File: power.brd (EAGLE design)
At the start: 73.3 x 52.1 mm, 21 parts

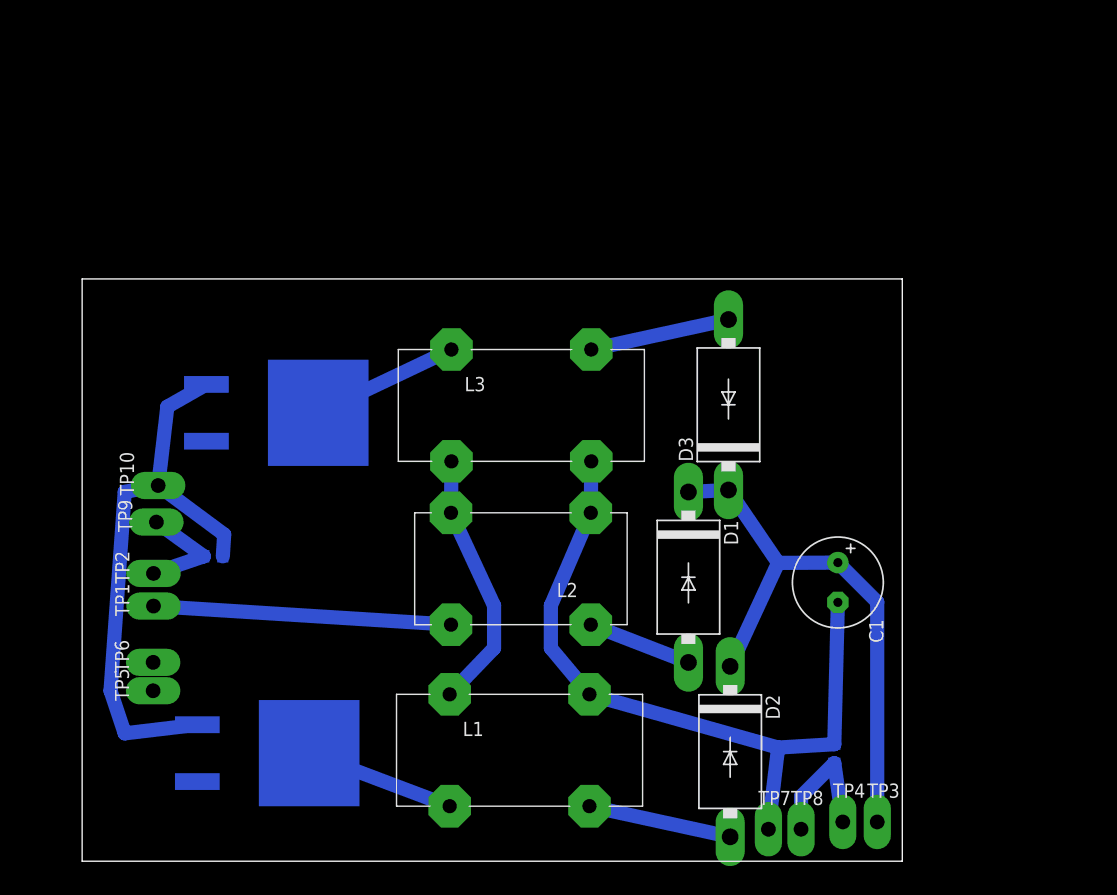
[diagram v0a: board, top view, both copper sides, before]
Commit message: Transformer footprints and really awful looking board routing
Pretty sure at least one of the transformers is wired in the wrong way
too
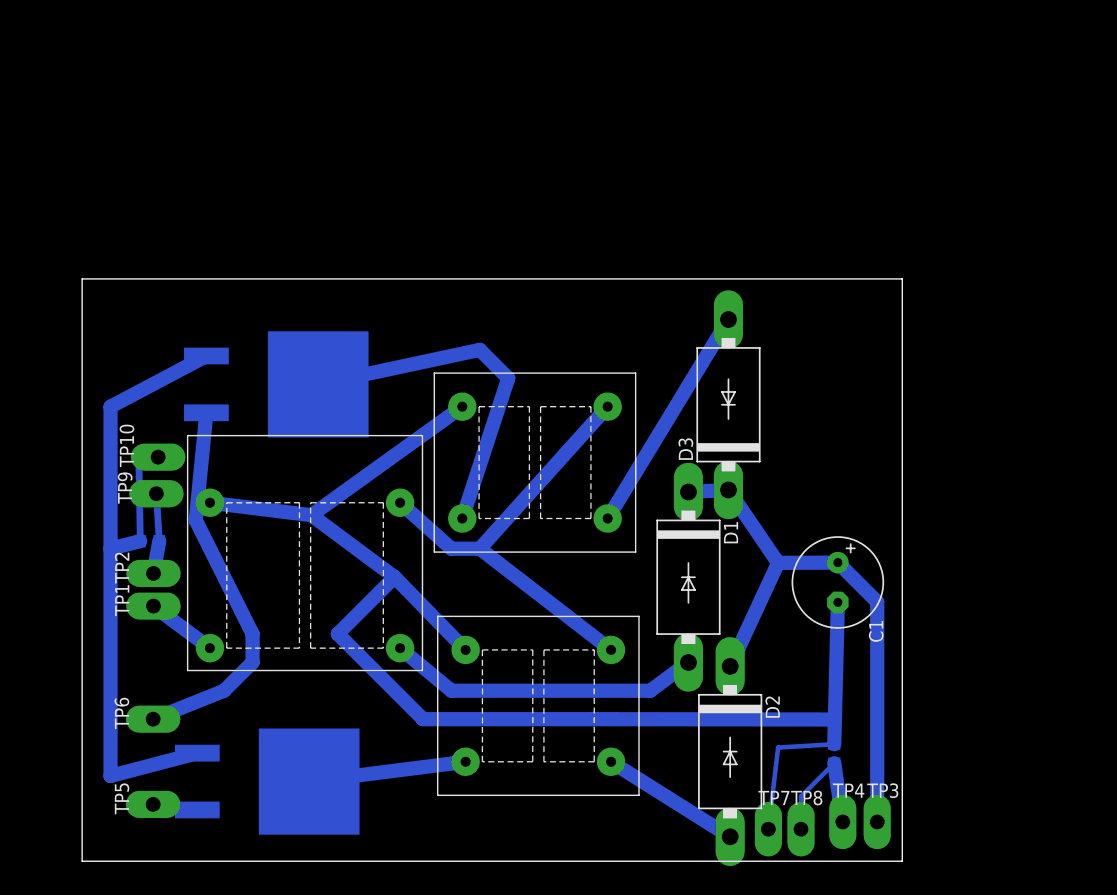
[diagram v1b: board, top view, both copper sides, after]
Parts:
- removed L1, L3: (no value), inductor-nkl:B2
- removed L2: (no value), inductor-nkl:B1
- added U$3: PLH10AN2211R5P2B, chokes:L13-17
- added U$4, U$5: TLF14CBH3321R0K1, chokes:L10-13
- moved TP5 10.2 mm to (1.27, 5.08)
- moved R2 5.84 mm to (0.97, 28.6), turned to 0 degrees
- moved TP6 5.08 mm to (1.27, 12.7)
- moved U$1 2.54 mm to (15.2, 7.12)
- moved TP10 2.54 mm to (1.72, 36.1)
- moved TP9 2.54 mm to (1.56, 32.9)
- moved U$2 2.54 mm to (16.0, 42.6)
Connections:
- removed net N$7: D2.A, L1.4
- new net N$15: U$1.P$3, U$5.P$1
- net N$1: now also U$3.P$2; no longer L2.1
- net N$2: now also D2.A, U$5.P$2; no longer L1.1, L2.4, L3.2
- net N$3: now also U$3.P$1; no longer L2.3
- net N$4: now also U$3.P$4, U$4.P$2, U$5.P$4; no longer L1.3, L2.2, L3.4
- net N$5: now also U$4.P$3; no longer L3.1
- net N$6: now also U$3.P$3, U$4.P$1, U$5.P$3; no longer L1.2, U$1.P$3
- net N$9: now also U$4.P$4; no longer L3.3
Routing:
- net N$4: track 65.4 -> 124.0 mm
- net N$13: track 0.00 -> 34.0 mm
- net N$6: track 13.4 -> 40.6 mm
- net N$3: track 26.7 -> 6.30 mm
- net N$1: track 9.36 -> 28.0 mm
- net N$5: track 13.2 -> 31.6 mm
- net N$15: track 0.00 -> 14.1 mm
- net N$7: track 12.9 -> 0.00 mm
- net N$2: track 23.3 -> 12.6 mm
- net N$11: track 51.8 -> 62.2 mm
- net N$9: track 12.6 -> 20.8 mm
- net N$10: track 9.98 -> 7.18 mm

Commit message: little tweaks
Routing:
- net N$4: track 124.0 -> 119.1 mm
- net N$12: track 0.00 -> 3.98 mm
- net N$11: track 62.2 -> 59.4 mm
- net N$6: track 40.6 -> 39.6 mm
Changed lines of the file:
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@@
 <wire x1="62.49" y1="23.142" x2="62.225715625" y2="12.6680625" width="1.27" layer="16"/>
 <wire x1="62.225715625" y1="12.6680625" x2="62.17" y2="10.46" width="1.27" layer="16"/>
-<wire x1="62.17" y1="10.46" x2="57.15" y2="10.16" width="0.4064" layer="16"/>
-<wire x1="57.15" y1="10.16" x2="56.28" y2="2.86" width="0.4064" layer="16"/>
+<wire x1="62.17" y1="10.46" x2="57.15" y2="7.62" width="0.4064" layer="16"/>
+<wire x1="57.15" y1="7.62" x2="56.28" y2="2.86" width="0.4064" layer="16"/>
 <contactref element="U$3" pad="P$4"/>
 <contactref element="U$5" pad="P$4"/>
 <contactref element="U$4" pad="P$2"/>
-<wire x1="29.21" y1="18.89" x2="22.86" y2="25.4" width="1.27" layer="16"/>
-<wire x1="22.86" y1="25.4" x2="15.423409375" y2="30.93535625" width="1.27" layer="16"/>
-<wire x1="15.423409375" y1="30.93535625" x2="6.35" y2="32.05" width="1.27" layer="16"/>
-<wire x1="28.91" y1="40.64" x2="15.423409375" y2="30.93535625" width="1.27" layer="16"/>
+<wire x1="29.21" y1="18.89" x2="20.32" y2="25.4" width="1.27" layer="16"/>
+<wire x1="20.32" y1="25.4" x2="17.963409375" y2="33.47535625" width="1.27" layer="16"/>
+<wire x1="17.963409375" y1="33.47535625" x2="6.35" y2="32.05" width="1.27" layer="16"/>
+<wire x1="28.91" y1="40.64" x2="17.963409375" y2="33.47535625" width="1.27" layer="16"/>
 <wire x1="40.64" y1="12.7" x2="25.4" y2="12.7" width="1.27" layer="16"/>
-<wire x1="25.4" y1="12.7" x2="17.78" y2="20.32" width="1.27" layer="16"/>
-<wire x1="17.78" y1="20.32" x2="22.86" y2="25.4" width="1.27" layer="16"/>
+<wire x1="25.4" y1="12.7" x2="20.32" y2="17.78" width="1.27" layer="16"/>
+<wire x1="20.32" y1="17.78" x2="20.32" y2="25.4" width="1.27" layer="16"/>
 <wire x1="40.64" y1="12.7" x2="62.225715625" y2="12.6680625" width="1.27" layer="16"/>
 </signal>
@@
 <contactref element="R2" pad="2"/>
 <contactref element="TP10" pad="TP"/>
-<wire x1="5.22" y1="9.66" x2="-2.54" y2="7.62" width="1.27" layer="16"/>
-<wire x1="-2.54" y1="7.62" x2="-2.54" y2="27.94" width="1.27" layer="16"/>
+<wire x1="5.22" y1="9.66" x2="-2.54" y2="10.16" width="1.27" layer="16"/>
+<wire x1="-2.54" y1="10.16" x2="-2.54" y2="27.94" width="1.27" layer="16"/>
 <wire x1="-2.54" y1="27.94" x2="-2.54" y2="40.64" width="1.27" layer="16"/>
 <wire x1="-2.54" y1="40.64" x2="6.03" y2="45.17" width="1.27" layer="16"/>
 <wire x1="0.12" y1="28.62" x2="-2.54" y2="27.94" width="1.27" layer="16"/>
-<wire x1="1.72" y1="36.13" x2="0" y2="35.56" width="0.6096" layer="16"/>
-<wire x1="0" y1="35.56" x2="0.12" y2="28.62" width="0.6096" layer="16"/>
+<wire x1="1.72" y1="36.13" x2="0" y2="35.56" width="0.4064" layer="16"/>
+<wire x1="0" y1="35.56" x2="0.12" y2="28.62" width="0.4064" layer="16"/>
 </signal>
 <signal name="N$12">
 <contactref element="TP5" pad="TP"/>
 <contactref element="U$1" pad="P$1"/>
-<wire x1="5.22" y1="4.58" x2="1.27" y2="5.08" width="0" layer="19" extent="16-16"/>
+<wire x1="1.27" y1="5.08" x2="5.22" y2="4.58" width="0.4064" layer="16"/>
 </signal>
 <signal name="N$13">
 <contactref element="TP6" pad="TP"/>
 <contactref element="U$2" pad="P$1"/>
-<wire x1="1.27" y1="12.7" x2="7.62" y2="15.24" width="1.27" layer="16"/>
-<wire x1="7.62" y1="15.24" x2="10.16" y2="17.78" width="1.27" layer="16"/>
-<wire x1="10.16" y1="17.78" x2="10.16" y2="20.32" width="1.27" layer="16"/>
-<wire x1="10.16" y1="20.32" x2="5.08" y2="30.48" width="1.27" layer="16"/>
-<wire x1="5.08" y1="30.48" x2="6.03" y2="40.09" width="1.27" layer="16"/>
+<wire x1="1.27" y1="12.7" x2="7.62" y2="15.24" width="0.4064" layer="16"/>
+<wire x1="7.62" y1="15.24" x2="10.16" y2="17.78" width="0.4064" layer="16"/>
+<wire x1="10.16" y1="17.78" x2="10.16" y2="20.32" width="0.4064" layer="16"/>
+<wire x1="10.16" y1="20.32" x2="5.08" y2="30.48" width="0.4064" layer="16"/>
+<wire x1="5.08" y1="30.48" x2="6.03" y2="40.09" width="0.4064" layer="16"/>
 </signal>
 <signal name="N$14">
@@
 <contactref element="TP2" pad="TP"/>
 <wire x1="1.3" y1="25.73" x2="1.82" y2="28.62" width="1.27" layer="16"/>
-<wire x1="1.56" y1="32.86" x2="1.82" y2="28.62" width="0.6096" layer="16"/>
+<wire x1="1.56" y1="32.86" x2="1.82" y2="28.62" width="0.4064" layer="16"/>
 </signal>
 <signal name="N$1">
@@
 <contactref element="U$4" pad="P$1"/>
 <wire x1="23.35" y1="32.05" x2="27.94" y2="27.94" width="1.27" layer="16"/>
-<wire x1="27.94" y1="27.94" x2="30.48" y2="27.94" width="1.27" layer="16"/>
-<wire x1="30.48" y1="27.94" x2="41.91" y2="40.64" width="1.27" layer="16"/>
-<wire x1="42.21" y1="18.89" x2="30.48" y2="27.94" width="1.27" layer="16"/>
+<wire x1="27.94" y1="27.94" x2="33.02" y2="27.94" width="1.27" layer="16"/>
+<wire x1="33.02" y1="27.94" x2="41.91" y2="40.64" width="1.27" layer="16"/>
+<wire x1="42.21" y1="18.89" x2="33.02" y2="27.94" width="1.27" layer="16"/>
 </signal>
 </signals>

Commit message: fiddling with the layout
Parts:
- moved TP3 7.62 mm to (66.0, 11.1)
- moved D3 5.68 mm to (55.2, 35.7)
- moved D2 5.68 mm to (55.4, 14.9)
- moved TP4 3.59 mm to (65.5, 6.05)
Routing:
- net N$8: track 51.7 -> 37.1 mm
- net N$9: track 20.8 -> 18.4 mm
- net N$14: track 12.4 -> 11.4 mm
- net N$2: track 12.6 -> 13.3 mm
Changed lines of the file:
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@@
 <?xml version="1.0" encoding="utf-8"?>
 <!DOCTYPE eagle SYSTEM "eagle.dtd">
-<eagle version="6.5.1">
+<eagle version="6.5.0">
 <drawing>
 <settings>
@@
 <setting verticaltext="up"/>
 </settings>
-<grid distance="0.1" unitdist="inch" unit="inch" style="lines" multiple="1" display="yes" altdistance="0.5" altunitdist="mm" altunit="mm"/>
+<grid distance="1" unitdist="mm" unit="mm" style="lines" multiple="5" display="yes" altdistance="0.5" altunitdist="mm" altunit="mm"/>
 <layers>
 <layer number="1" name="Top" color="4" fill="1" visible="yes" active="yes"/>
@@
 <attribute name="TP_SIGNAL_NAME" value="" x="19.08" y="47.32" size="1.778" layer="27" rot="R90" display="off"/>
 </element>
-<element name="TP3" library="testpad" package="P1-13Y" value="TPPAD1-13Y" x="66.01" y="3.51">
-<attribute name="TP_SIGNAL_NAME" value="" x="92.68" y="-14.27" size="1.778" layer="27" display="off"/>
-</element>
-<element name="TP4" library="testpad" package="P1-13Y" value="TPPAD1-13Y" x="62.93" y="3.51">
-<attribute name="TP_SIGNAL_NAME" value="" x="94.68" y="-14.27" size="1.778" layer="27" display="off"/>
+<element name="TP3" library="testpad" package="P1-13Y" value="TPPAD1-13Y" x="66.01" y="11.13">
+<attribute name="TP_SIGNAL_NAME" value="" x="92.68" y="-6.65" size="1.778" layer="27" display="off"/>
+</element>
+<element name="TP4" library="testpad" package="P1-13Y" value="TPPAD1-13Y" x="65.47" y="6.05">
+<attribute name="TP_SIGNAL_NAME" value="" x="97.22" y="-11.73" size="1.778" layer="27" display="off"/>
 </element>
 <element name="TP5" library="testpad" package="P1-13Y" value="TPPAD1-13Y" x="1.27" y="5.08" rot="R90">
@@
 </element>
 <element name="D1" library="diode" package="DO201-15" value="BY500" x="49.13" y="25.39" rot="R270"/>
-<element name="D2" library="diode" package="DO201-15" value="BY500" x="52.86" y="9.8" rot="R270"/>
-<element name="D3" library="diode" package="DO201-15" value="BY500" x="52.71" y="40.81" rot="R90"/>
+<element name="D2" library="diode" package="DO201-15" value="BY500" x="55.4" y="14.88" rot="R270"/>
+<element name="D3" library="diode" package="DO201-15" value="BY500" x="55.25" y="35.73" rot="R90"/>
 <element name="C1" library="rcl" package="E3,5-8" value="" x="62.49" y="24.92" rot="R270"/>
 <element name="U$1" library="mjg" package="TO-263AB" value="FDB6670AL" x="15.22" y="7.12" rot="MR90"/>
@@
 <contactref element="C1" pad="+"/>
 <contactref element="D3" pad="C"/>
-<wire x1="49.13" y1="33.01" x2="52.71" y2="33.19" width="1.27" layer="16"/>
+<wire x1="49.13" y1="33.01" x2="55.25" y2="28.11" width="1.27" layer="16"/>
 <wire x1="62.49" y1="26.698" x2="66.01" y2="23.178" width="1.27" layer="16"/>
-<wire x1="66.01" y1="23.178" x2="66.01" y2="3.51" width="1.27" layer="16"/>
-<wire x1="52.71" y1="33.19" x2="57.15" y2="26.67" width="1.27" layer="16"/>
-<wire x1="57.15" y1="26.67" x2="52.86" y2="17.42" width="1.27" layer="16"/>
+<wire x1="66.01" y1="23.178" x2="66.01" y2="11.13" width="1.27" layer="16"/>
+<wire x1="55.25" y1="28.11" x2="57.15" y2="26.67" width="1.27" layer="16"/>
+<wire x1="57.15" y1="26.67" x2="55.4" y2="22.5" width="1.27" layer="16"/>
 <wire x1="57.15" y1="26.67" x2="62.49" y2="26.698" width="1.27" layer="16"/>
 </signal>
@@
 <contactref element="D3" pad="A"/>
 <contactref element="U$4" pad="P$4"/>
-<wire x1="41.91" y1="30.64" x2="52.71" y2="48.43" width="1.27" layer="16"/>
+<wire x1="41.91" y1="30.64" x2="55.25" y2="43.35" width="1.27" layer="16"/>
 </signal>
 <signal name="N$5">
@@
 <contactref element="R1" pad="2"/>
 <contactref element="TP8" pad="TP"/>
-<wire x1="62.17" y1="8.76" x2="62.93" y2="3.51" width="1.27" layer="16"/>
+<wire x1="62.17" y1="8.76" x2="65.47" y2="6.05" width="1.27" layer="16"/>
 <wire x1="59.2" y1="2.86" x2="59.2" y2="5.79" width="0.4064" layer="16"/>
 <wire x1="59.2" y1="5.79" x2="62.17" y2="8.76" width="0.4064" layer="16"/>
@@
 <contactref element="D2" pad="A"/>
 <contactref element="U$5" pad="P$2"/>
-<wire x1="52.86" y1="2.18" x2="42.21" y2="8.89" width="1.27" layer="16"/>
+<wire x1="55.4" y1="7.26" x2="42.21" y2="8.89" width="1.27" layer="16"/>
 </signal>
 <signal name="N$15">

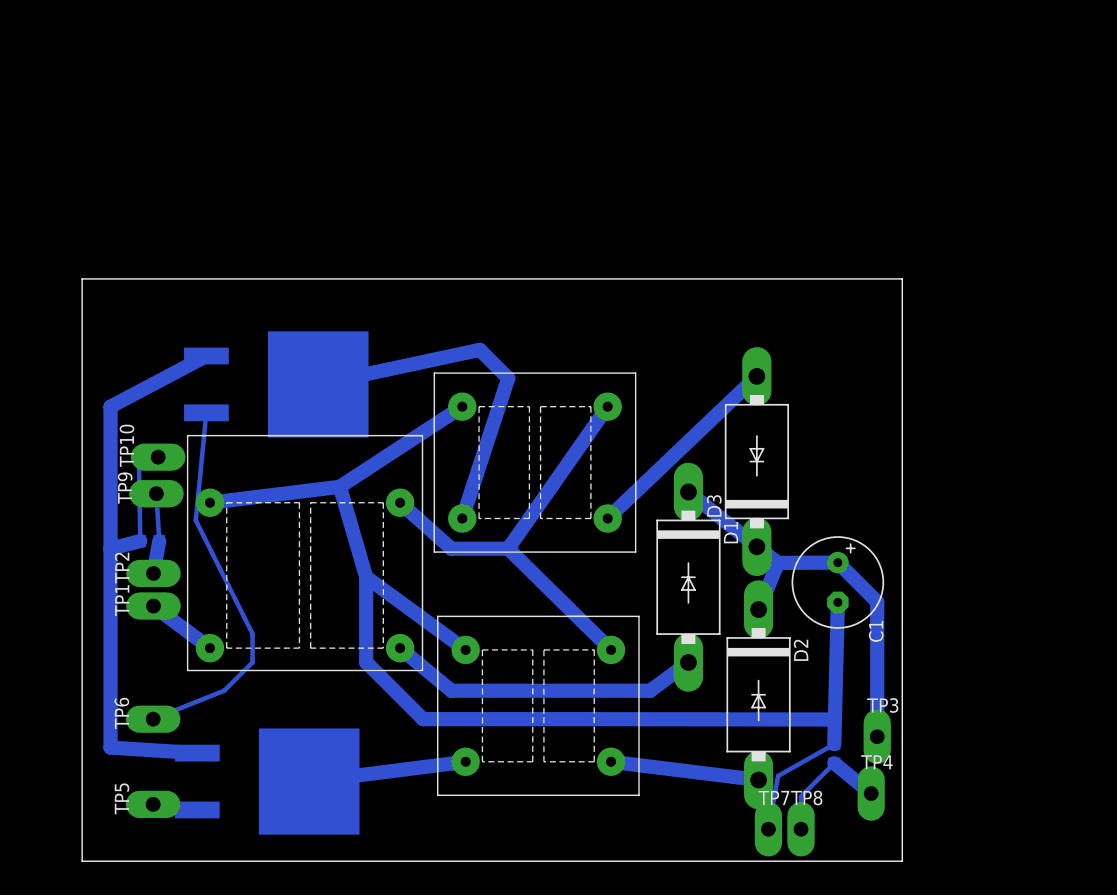
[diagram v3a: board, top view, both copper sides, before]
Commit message: proposed beaglebone connections and resistor dividers
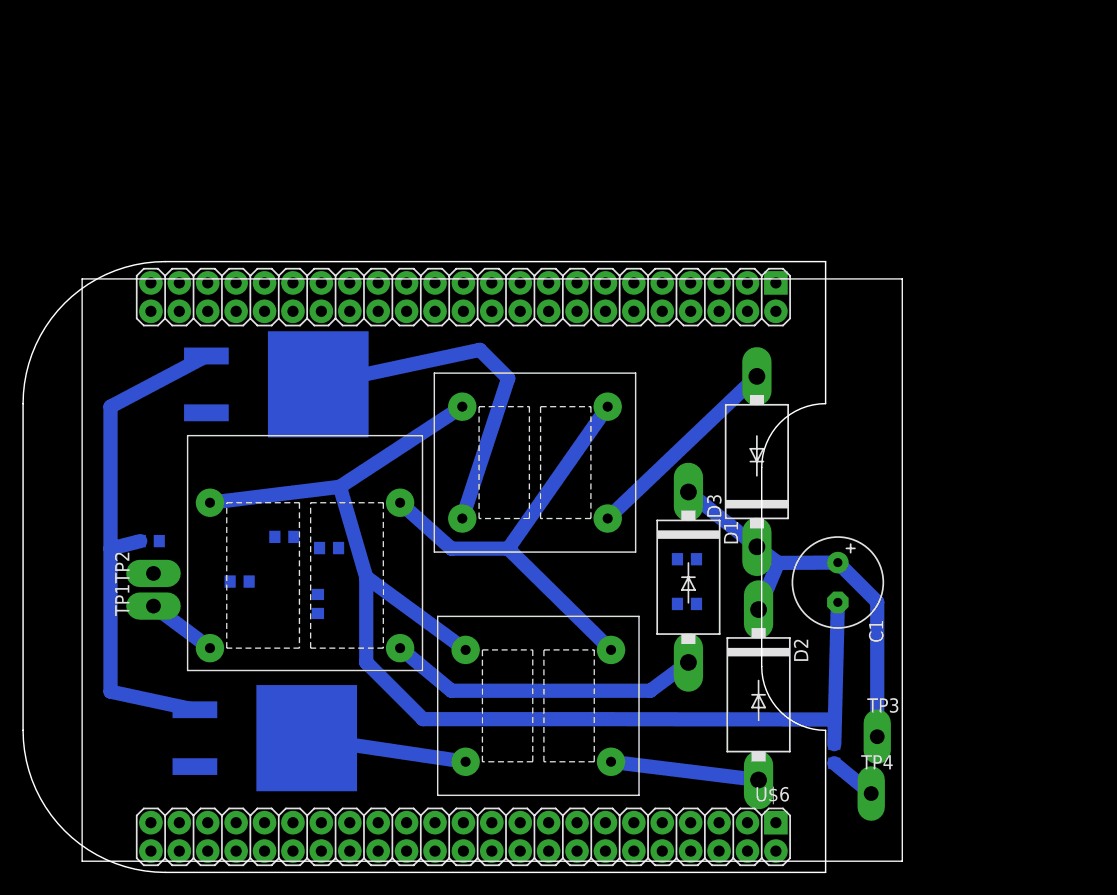
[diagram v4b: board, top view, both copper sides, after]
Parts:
- removed TP10, TP5, TP6, TP7, TP8, TP9: TPPAD1-13Y, testpad:P1-13Y
- added R3, R5: 47k, rcl:R0603
- added R4, R6, R8: 1k, rcl:R0603
- added R7: 15k, rcl:R0603
- added U$6: BEAGLEBONE_OUTLINE, adafruit:BEAGLEBONE_SHIELD
- moved U$1 3.89 mm to (15.0, 11.0)
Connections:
- removed net N$8: C1.+, D1.C, D2.C, D3.C, TP3.TP
- new net GND: C1.-, R1.1, R4.1, R6.1, R8.1, U$3.P$4, U$4.P$2, U$5.P$4, U$6.1, U$6.2, U$6.47, U$6.48, U$6.89, U$6.90, U$6.91, U$6.92
- new net N$16: R2.1, R5.1, TP2.TP
- new net N$17: R5.2, R6.2, U$6.86
- new net N$7: C1.+, D1.C, D2.C, D3.C, R7.1, TP3.TP
- new net SYS_5V: U$6.53
- new net VDD_3V3EXP: U$6.49, U$6.50
- new net VDD_5V: U$6.51, U$6.52
- net N$10: now also R7.2, R8.2, U$6.84; no longer R2.1, TP2.TP, TP9.TP
- net N$11: no longer TP10.TP
- net N$12: now also U$6.77; no longer TP5.TP
- net N$13: now also U$6.75; no longer TP6.TP
- net N$14: now also U$6.83; no longer TP8.TP
- net N$3: now also R3.1
- net N$4: now also R3.2, R4.2, U$6.85; no longer C1.-, R1.1, TP7.TP, U$3.P$4, U$4.P$2, U$5.P$4
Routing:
- net N$4: track 119.1 -> 0.00 mm
- net GND: track 0.00 -> 108.5 mm
- net N$8: track 37.1 -> 0.00 mm
- net N$7: track 0.00 -> 37.1 mm
- net N$13: track 34.0 -> 0.00 mm
- net N$11: track 59.4 -> 45.6 mm
- net N$10: track 7.18 -> 0.00 mm
- net N$14: track 11.4 -> 4.27 mm
- net N$12: track 3.98 -> 0.00 mm
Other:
- board size 73.3 x 52.1 mm -> 71.8 x 54.6 mm

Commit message: change all the things
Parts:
- removed TP1, TP2, TP3, TP4: TPPAD1-13Y, testpad:P1-13Y
- added BAT+, BAT-, H1, H2, PV+, PV-: MOUNT-PAD-ROUND2.8, holes:2,8-PAD
- added R10: 1k, rcl:R0603
- added R9: 47k, rcl:R0603
- R1, R2: value (none) -> 0R1
- moved U$6 101.4 mm to (-1.00, 65.0), turned to 270 degrees
- moved U$3 43.8 mm to (42.0, 44.6), flipped to the bottom, turned to 270 degrees
- moved R1 30.1 mm to (73.2, 37.6)
- moved R2 27.3 mm to (25.0, 41.6)
- moved D1 26.8 mm to (75.0, 32.5), turned to 180 degrees
- moved D3 25.9 mm to (75.0, 52.5), turned to 180 degrees
- moved C1 21.5 mm to (74.9, 42.5), turned to 180 degrees
- moved D2 21.0 mm to (75.0, 22.5), turned to 180 degrees
- moved R3 20.9 mm to (29.0, 31.0), turned to 180 degrees
- moved R7 20.6 mm to (67.0, 37.0)
- moved R8 20.6 mm to (67.0, 33.0)
- moved U$5 20.6 mm to (47.2, 18.9)
- moved R6 18.0 mm to (32.0, 38.0)
- moved R4 17.5 mm to (32.0, 30.0)
- moved R5 16.6 mm to (27.0, 38.0)
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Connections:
- new net N$18: R10.2, R9.2, U$6.79
- new net N$8: R9.1
- net GND: now also H1.B2,8, H2.B2,8, R10.1
- net N$14: now also BAT-.B2,8; no longer TP4.TP
- net N$16: now also PV-.B2,8; no longer TP2.TP
- net N$3: now also PV+.B2,8, U$3.P$3; no longer TP1.TP, U$3.P$1
- net N$6: now also U$3.P$1; no longer U$3.P$3
- net N$7: now also BAT+.B2,8; no longer TP3.TP
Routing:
- net GND: track 108.5 -> 0.00 mm
- net N$11: track 45.6 -> 0.00 mm
- net N$6: track 39.6 -> 0.00 mm
- net N$7: track 37.1 -> 0.00 mm
- net N$5: track 31.6 -> 0.00 mm
- net N$1: track 28.0 -> 0.00 mm
- net N$9: track 18.4 -> 0.00 mm
- net N$15: track 14.4 -> 0.00 mm
- net N$2: track 13.3 -> 0.00 mm
- net N$3: track 6.30 -> 0.00 mm
- net N$14: track 4.27 -> 0.00 mm
- added copper zone on layer 16, net GND
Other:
- board size 71.8 x 54.6 mm -> 85 x 75 mm
